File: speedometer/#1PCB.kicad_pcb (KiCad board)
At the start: 2 copper layers, 70 parts, among them J1 Conn_01x02, J2 CAN to outer connector, J3 DTF13-6P, U1 A1104xLH, U2 NE555P, U3 A1104xLH, U4 NE555P, U5 A1104xLH, U6 NE555P, U7 MCP2515-I, U8 TJA1050DRG, X1 8MHz

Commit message: aw hell naw
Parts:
- removed J1: Conn_01x02, Connector_Wire:SolderWire-0.75sqmm_1x02_P4.8mm_D1.25mm_OD2.3mm
- removed J2: CAN to outer connector, Connector_Wire:SolderWire-0.1sqmm_1x04_P3.6mm_D0.4mm_OD1mm
- added REF**: MountingHole_3.5mm, MountingHole:MountingHole_3.5mm, F.Cu at (129.2, 24.1)
- added REF**: MountingHole_3.5mm, MountingHole:MountingHole_3.5mm, F.Cu at (30.7, 24.1)
- added REF**: MountingHole_3.5mm, MountingHole:MountingHole_3.5mm, F.Cu at (129.2, 90.6)
- added REF**: MountingHole_3.5mm, MountingHole:MountingHole_3.5mm, F.Cu at (30.7, 90.6)
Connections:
- A1 pad 5: unconnected-(A1-D2-Pad5) -> INT
- U7 pad 12: unconnected-(U7-~{INT}-Pad12) -> INT
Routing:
- net INT: track 0.00 -> 84.0 mm, vias 0 -> 1
- net High: track 161.7 -> 129.0 mm
- net Low: track 164.8 -> 132.7 mm, vias 4 -> 3
- net GND: track 134.9 -> 105.3 mm
- net +5V: track 495.8 -> 485.4 mm
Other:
- board outline added: 111.5 x 79.4 mm

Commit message: Add F points
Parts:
- added ?: , , F.Cu at (131.0, 84.0)
- added ?: , , F.Cu at (30.5, 83.5)
- added ?: , , F.Cu at (30.5, 29.5)
- added REF**: Fiducial_0.75mm_Mask1.5mm, Fiducial:Fiducial_0.75mm_Mask1.5mm, F.Cu at (129.5, 30.0)
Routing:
- net INT: track 84.0 -> 81.8 mm
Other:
- board text added: "PCB Designed By Zoe Stokes"

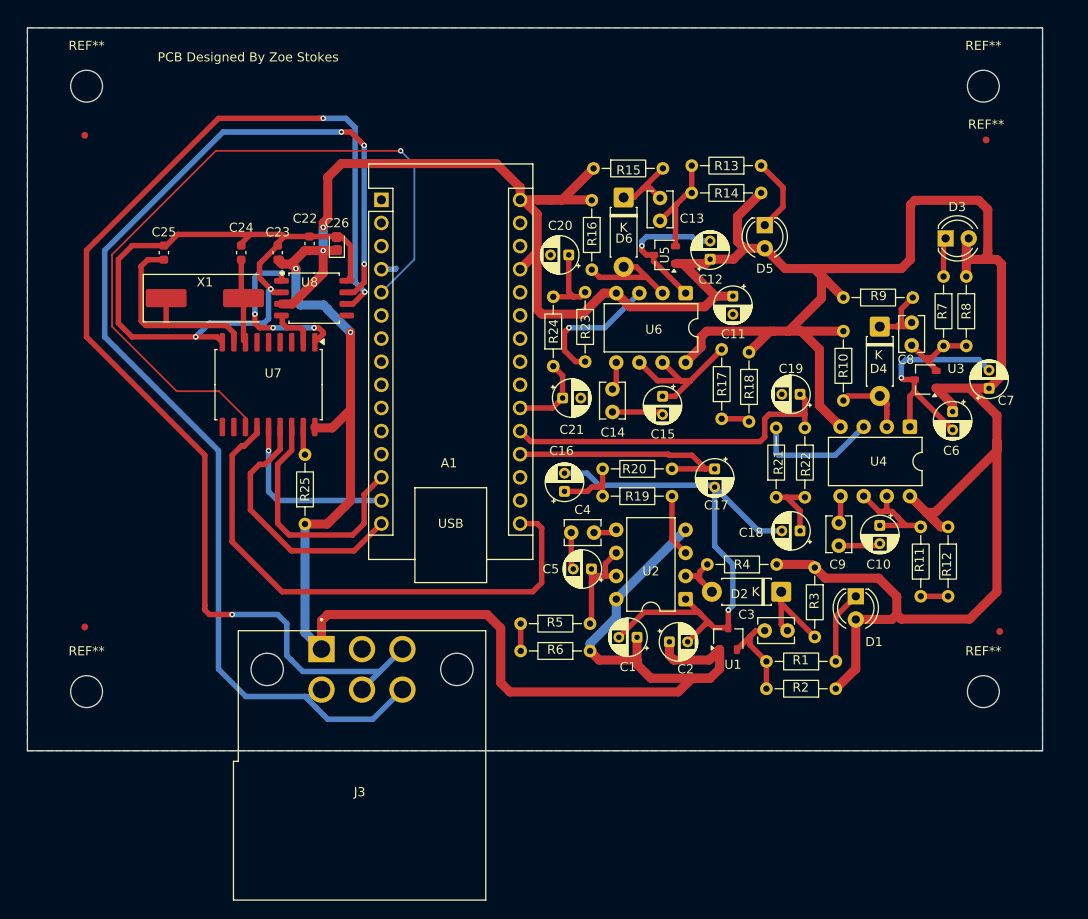
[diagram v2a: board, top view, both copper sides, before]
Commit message: Fixed the speedometer silly
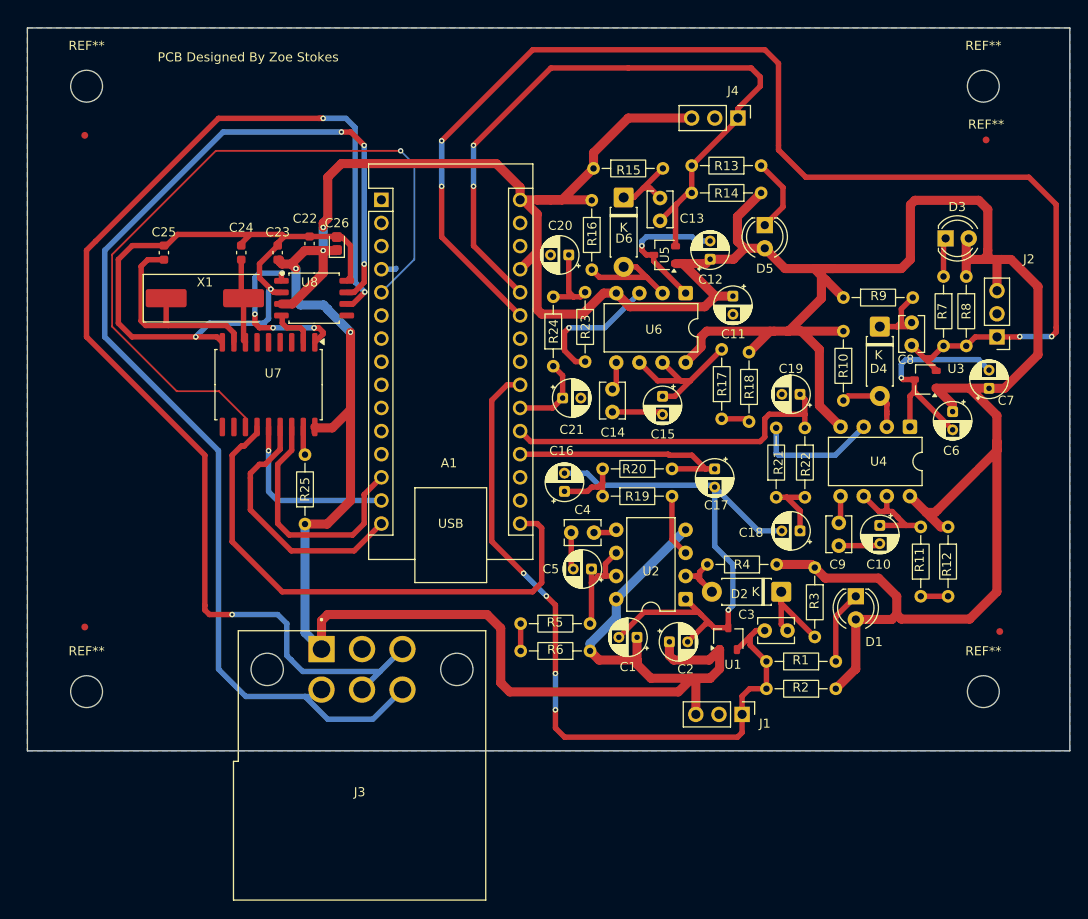
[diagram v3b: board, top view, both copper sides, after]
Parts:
- added J1: Hall1, Connector_PinHeader_2.54mm:PinHeader_1x03_P2.54mm_Vertical, F.Cu at (102.7, 93.1)
- added J2: Hall2, Connector_PinHeader_2.54mm:PinHeader_1x03_P2.54mm_Vertical, F.Cu at (130.7, 51.6)
- added J4: Hall3, Connector_PinHeader_2.54mm:PinHeader_1x03_P2.54mm_Vertical, F.Cu at (102.2, 27.6)
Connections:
- A1 pad 22: unconnected-(A1-A3-Pad22) -> Hall1_IN
- A1 pad 25: unconnected-(A1-A6-Pad25) -> Hall2_IN
- A1 pad 26: unconnected-(A1-A7-Pad26) -> Hall3_IN
- C13 pad 2: Net-(U5-V_{OUT}) -> Hall3_IN
- C3 pad 2: Net-(U1-V_{OUT}) -> Hall1_IN
- C8 pad 2: Net-(U3-V_{OUT}) -> Hall2_IN
- R1 pad 2: Net-(U1-V_{OUT}) -> Hall1_IN
- R13 pad 2: Net-(U5-V_{OUT}) -> Hall3_IN
- R14 pad 2: Net-(U5-V_{OUT}) -> Hall3_IN
- R2 pad 2: Net-(U1-V_{OUT}) -> Hall1_IN
- R7 pad 2: Net-(U3-V_{OUT}) -> Hall2_IN
- R8 pad 2: Net-(U3-V_{OUT}) -> Hall2_IN
- U1 pad 2: Net-(U1-V_{OUT}) -> Hall1_IN
- U3 pad 2: Net-(U3-V_{OUT}) -> Hall2_IN
- U5 pad 2: Net-(U5-V_{OUT}) -> Hall3_IN
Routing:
- net Hall2_IN: track 0.00 -> 140.6 mm, vias 0 -> 4
- net Hall1_IN: track 0.00 -> 81.3 mm, vias 0 -> 4
- net Hall3_IN: track 0.00 -> 79.0 mm, vias 0 -> 2
- net +5V: track 485.4 -> 512.5 mm
- net Net-(U5-V_{OUT}): track 12.5 -> 0.00 mm
- net Net-(U1-V_{OUT}): track 10.4 -> 0.00 mm
- net Net-(U3-V_{OUT}): track 9.09 -> 0.00 mm
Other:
- board size 111.5 x 79.4 mm -> 114.5 x 79.4 mm
